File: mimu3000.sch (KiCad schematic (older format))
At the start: 14 parts, among them SW1 P_MISO, SW2 P_MOSI, U1 ATTINY13A-SSU, U2 H11F1M

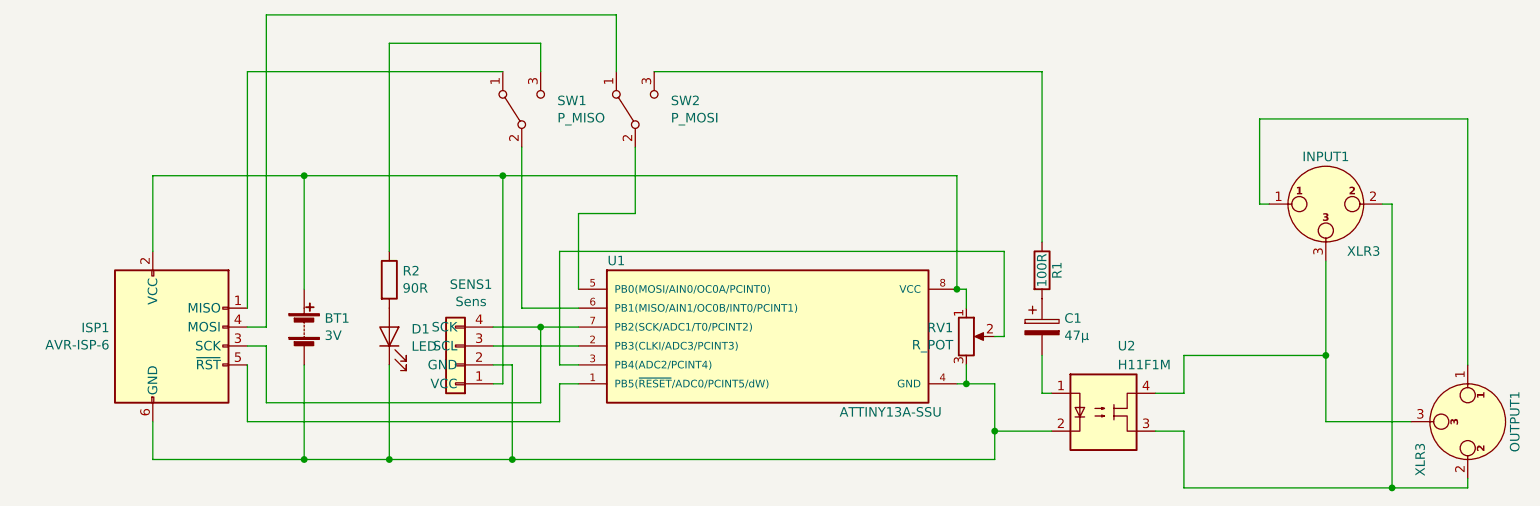
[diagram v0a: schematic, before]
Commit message: Updated to using new low R_on optocoupler
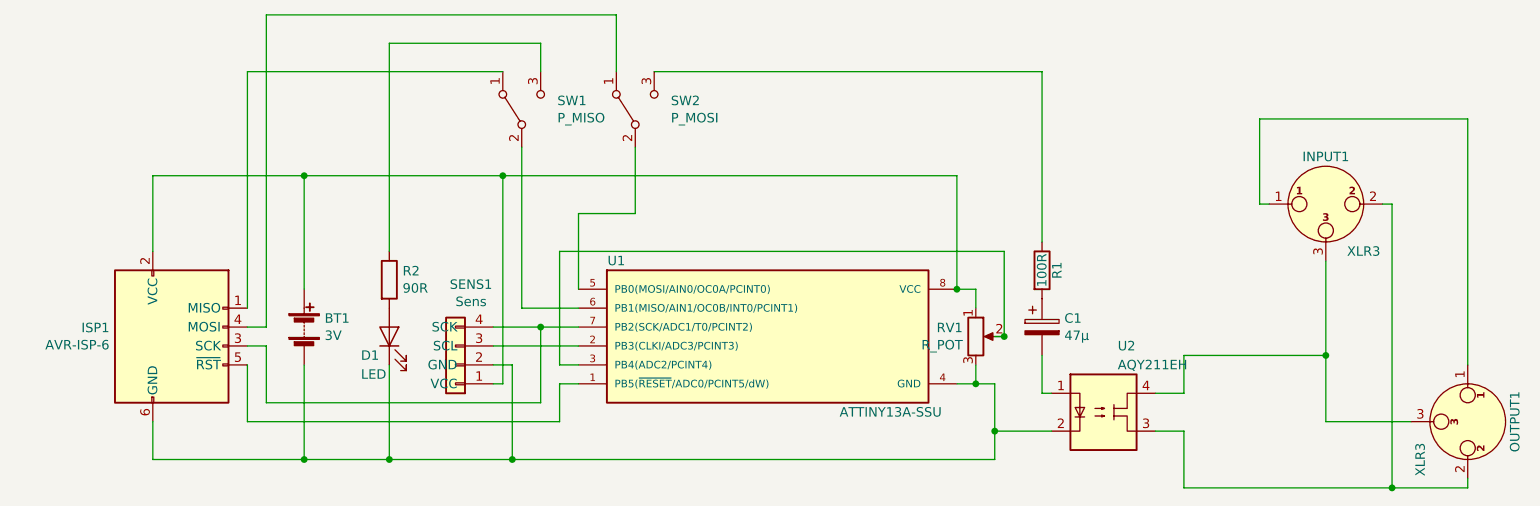
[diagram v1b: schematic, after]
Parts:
- U2: value H11F1M -> AQY211EH; footprint Package_DIP:DIP-6_W7.62mm -> Package_DIP:DIP-4_W7.62mm
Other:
- moved on the sheet: RV1
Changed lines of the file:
@@
 	8150 2750 7050 2750
 Wire Wire Line
-	5650 4150 5500 4150
+	5650 4150 5550 4150
 Connection ~ 7400 4000
 Connection ~ 7750 4700
@@
 	6650 4000 6650 4200
 Wire Wire Line
-	6650 4200 6500 4200
-Wire Wire Line
 	7400 4000 6650 4000
-Wire Wire Line
-	6500 4400 6650 4400
 Wire Wire Line
 	6650 4400 6650 4700
@@
 P 6250 4300
 F 0 "U2" H 6300 4650 50  0000 L CNN
-F 1 "H11F1M" H 6300 4550 50  0000 L CNN
-F 2 "Package_DIP:DIP-6_W7.62mm" H 6200 4300 50  0001 C CNN
-F 3 "https://www.mouser.com/datasheet/2/149/h11f1m-185284.pdf" H 6200 4300 50  0001 C CNN
+F 1 "AQY211EH" H 6300 4550 50  0000 L CNN
+F 2 "Package_DIP:DIP-4_W7.62mm" H 6200 4300 50  0001 C CNN
+F 3 "doc/semi_eng_ge1a_aqy21_e.pdf" H 6200 4300 50  0001 C CNN
 	1    6250 4300
 	1    0    0    -1
@@
 L Device:R_POT RV1
 U 1 1 5E2BA12E
-P 5500 3900
-F 0 "RV1" H 5431 3946 50  0000 R CNN
-F 1 "R_POT" H 5431 3855 50  0000 R CNN
-F 2 "Potentiometer_THT:Potentiometer_Alps_RK09Y11_Single_Horizontal" H 5500 3900 50  0001 C CNN
-F 3 "~" H 5500 3900 50  0001 C CNN
-	1    5500 3900
-	1    0    0    -1
-$EndComp
-Wire Wire Line
-	5500 4150 5500 4050
-Connection ~ 5500 4150
-Wire Wire Line
-	5500 4150 5450 4150
-Wire Wire Line
-	5500 3750 5500 3650
-Wire Wire Line
-	5500 3650 5450 3650
+P 5550 3900
+F 0 "RV1" H 5481 3946 50  0000 R CNN
+F 1 "R_POT" H 5481 3855 50  0000 R CNN
+F 2 "Potentiometer_THT:Potentiometer_Alps_RK09Y11_Single_Horizontal" H 5550 3900 50  0001 C CNN
+F 3 "~" H 5550 3900 50  0001 C CNN
+	1    5550 3900
+	1    0    0    -1
+$EndComp
+Connection ~ 5550 4150
 Connection ~ 5450 3650
 Wire Wire Line
@@
 U 1 1 5E2C9905
 P 2450 3900
-F 0 "D1" V 2489 3783 50  0000 R CNN
-F 1 "LED" V 2398 3783 50  0000 R CNN
+F 0 "D1" V 2350 4050 50  0000 R CNN
+F 1 "LED" V 2250 4050 50  0000 R CNN
 F 2 "LED_THT:LED_D3.0mm" H 2450 3900 50  0001 C CNN
 F 3 "~" H 2450 3900 50  0001 C CNN
@@
 Wire Wire Line
 	1800 2200 1800 3850
+Wire Wire Line
+	6500 4200 6650 4200
+Wire Wire Line
+	6500 4400 6650 4400
+Connection ~ 5700 3900
+Wire Wire Line
+	5550 4050 5550 4150
+Wire Wire Line
+	5450 4150 5550 4150
+Wire Wire Line
+	5550 3750 5550 3650
+Wire Wire Line
+	5450 3650 5550 3650
 $EndSCHEMATC
